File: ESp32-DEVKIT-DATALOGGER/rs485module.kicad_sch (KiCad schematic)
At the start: 17 parts, among them J301 RJ45, U301 MAX485E, U302 MAX3486

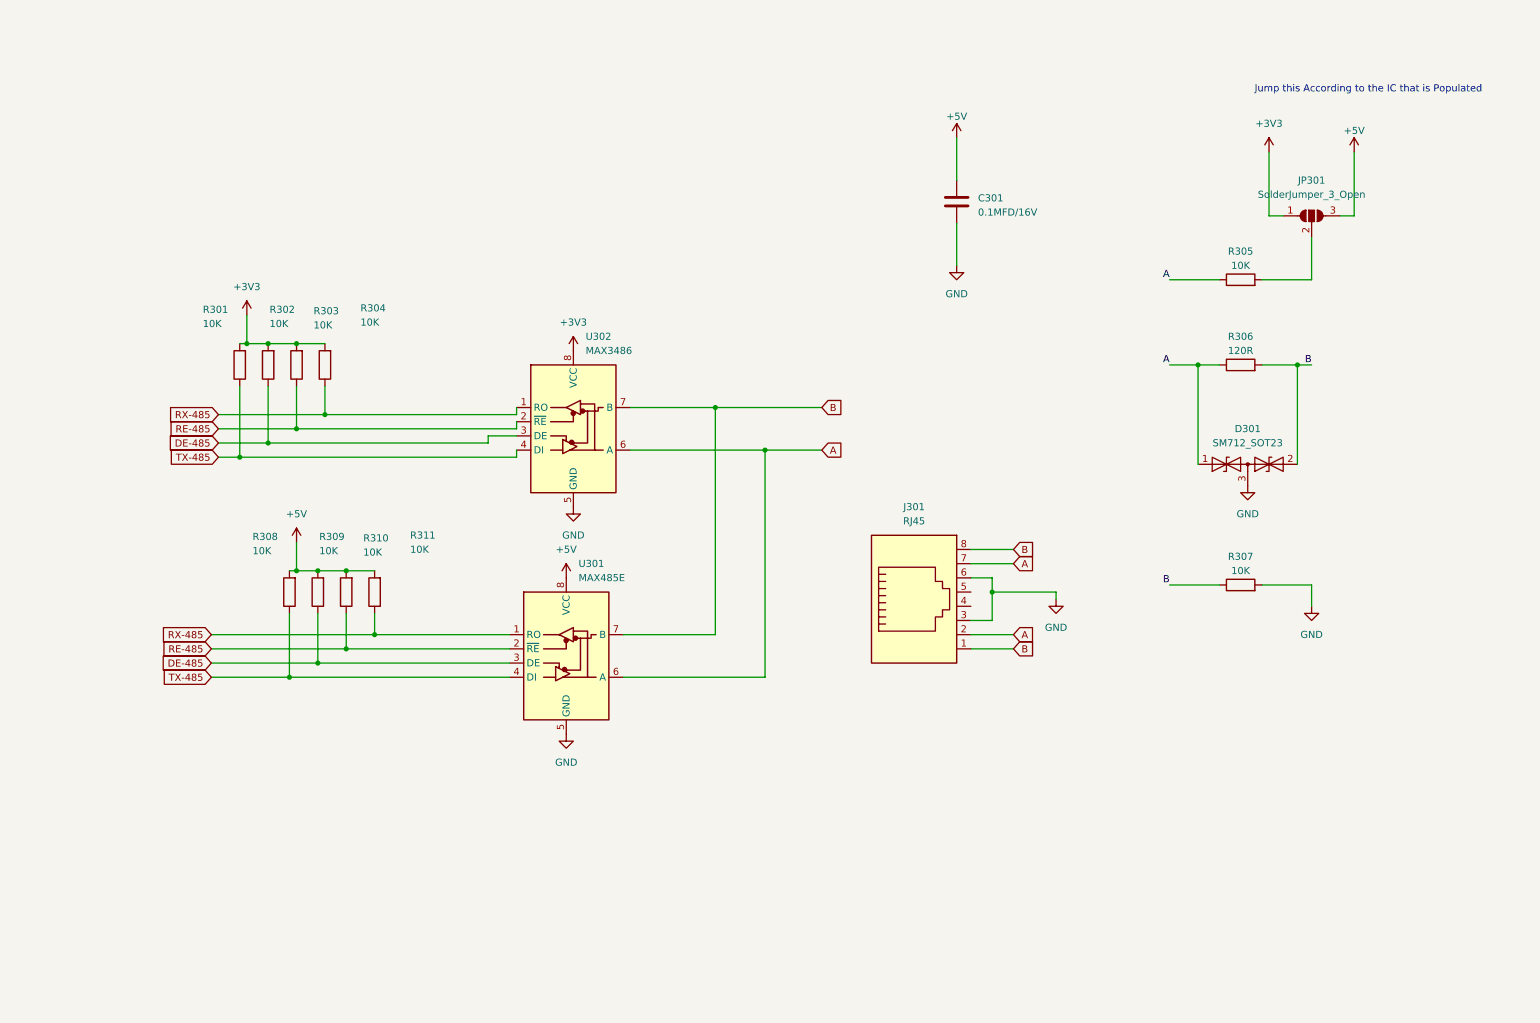
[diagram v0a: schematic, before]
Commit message: Small Changes
Adding I2C components
More RS485
And it is required changing the  Labels for RS485 . for 3 different channels
And Make them ISO Pins
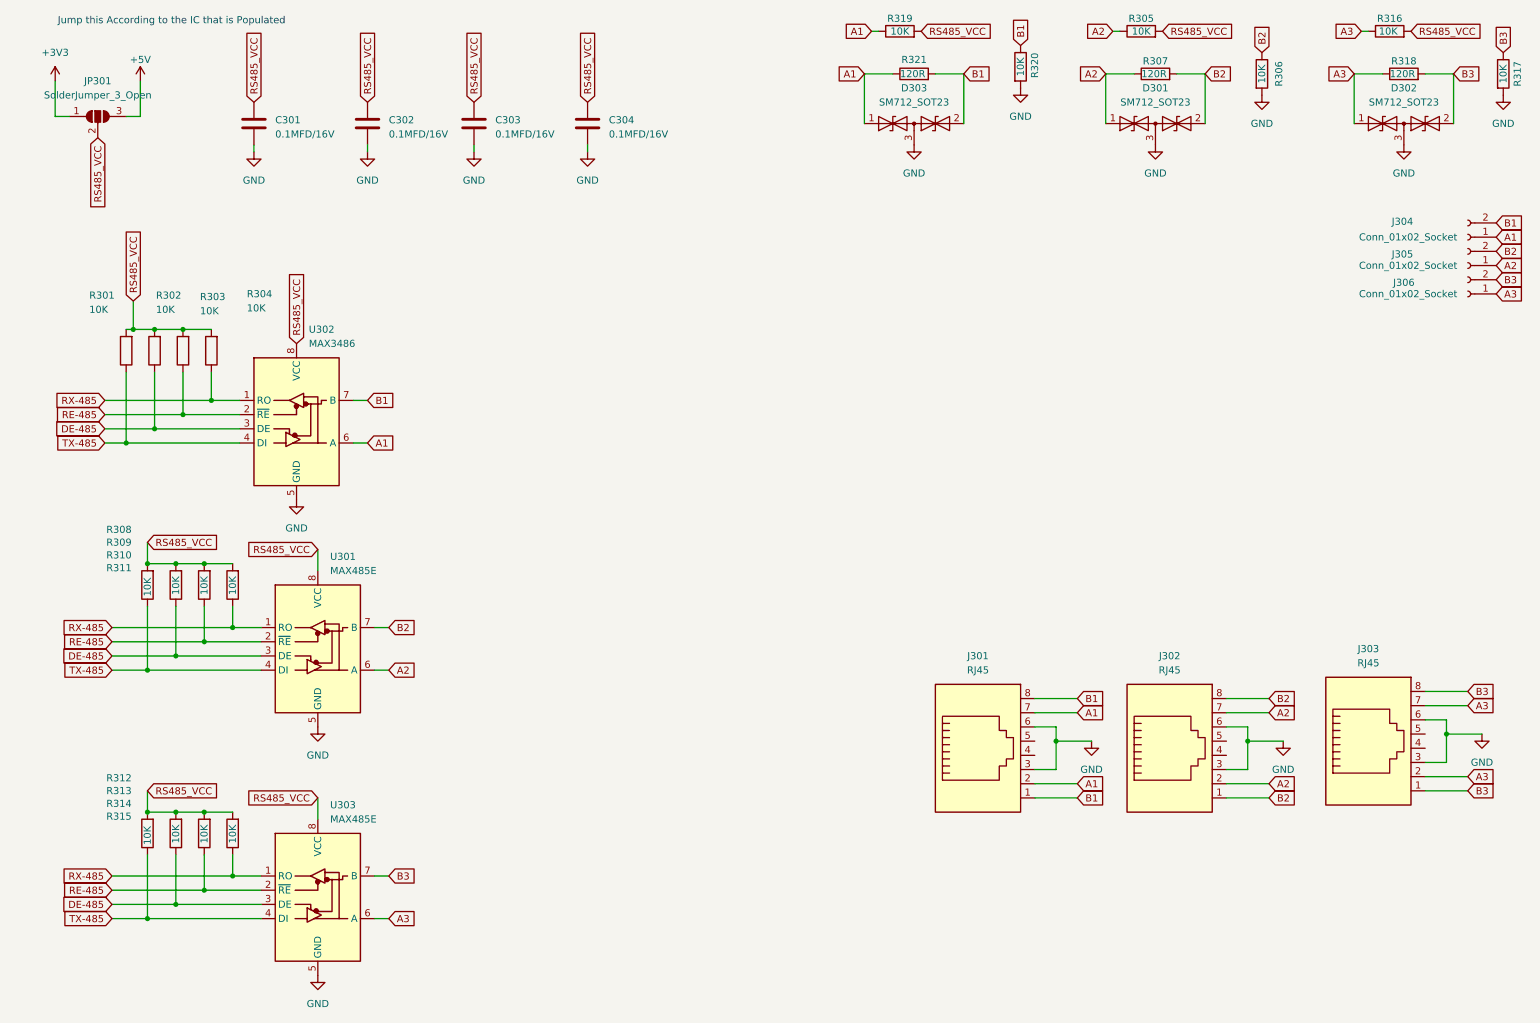
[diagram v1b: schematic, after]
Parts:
- added C302, C303, C304: 0.1MFD/16V, Capacitor_SMD:C_0603_1608Metric_Pad1.08x0.95mm_HandSolder, symbol Device:C
- added D302, D303: SM712_SOT23, Package_TO_SOT_SMD:SOT-23, symbol Diode:SM712_SOT23
- added J302, J303: RJ45, Connector_RJ:RJ45_Amphenol_54602-x08_Horizontal, symbol Connector:RJ45
- added J304, J305, J306: Conn_01x02_Socket, Connector_Molex:Molex_KK-254_AE-6410-02A_1x02_P2.54mm_Vertical, symbol Connector:Conn_01x02_Socket
- added R312, R313, R314, R315, R316, R317, R319, R320: 10K, Resistor_SMD:R_0603_1608Metric_Pad0.98x0.95mm_HandSolder, symbol Device:R
- added R318, R321: 120R, Resistor_SMD:R_0603_1608Metric_Pad0.98x0.95mm_HandSolder, symbol Device:R
- added U303: MAX485E, Package_DIP:DIP-8_W7.62mm_LongPads, symbol Interface_UART:MAX485E
- R306: value 120R -> 10K
- R307: value 10K -> 120R
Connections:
- net +3V3: no longer R301.2, R302.2, R303.2, R304.2, U302.8 (VCC)
- net +5V: no longer C301.1, R308.2, R309.2, R310.2, R311.2, U301.8 (VCC)
- net DE-485: now also R313.1, U303.3 (DE)
- net GND: now also R306.2, C302.2, C303.2, C304.2, D302.3 (common), D303.3 (common), J302.3, J302.6, J303.3, J303.6, R317.2, R320.2, U303.5 (GND); no longer R307.2
- net RE-485: now also R314.1, U303.2 (~{RE})
- net RX-485: now also R315.1, U303.1 (RO)
- net TX-485: now also R312.1, U303.4 (DI)
- net RS485_VCC: now reaches JP301.2 (C), R305.2
- net RS485_VCC: now also C301.1, R301.2, R302.2, R303.2, R304.2, R308.2, R309.2, R310.2, R311.2, U301.8 (VCC), U302.8 (VCC), C302.1, C303.1, C304.1, R312.2, R313.2, R314.2, R315.2, R316.2, R319.2, U303.8 (VCC)
- removed net A: D301.1 (A1), J301.2, J301.7, R305.1, R306.1, U301.6 (A), U302.6 (A)
- removed net B: D301.2 (A2), J301.1, J301.8, R306.2, R307.1, U301.7 (B), U302.7 (B)
- new net A1: D303.1 (A1), J301.2, J301.7, J304.1 (Pin_1), R319.1, R321.1, U302.6 (A)
- new net A2: D301.1 (A1), J302.2, J302.7, J305.1 (Pin_1), R305.1, R307.1, U301.6 (A)
- new net A3: D302.1 (A1), J303.2, J303.7, J306.1 (Pin_1), R316.1, R318.1, U303.6 (A)
- new net B1: D303.2 (A2), J301.1, J301.8, J304.2 (Pin_2), R320.1, R321.2, U302.7 (B)
- new net B2: D301.2 (A2), J302.1, J302.8, J305.2 (Pin_2), R306.1, R307.2, U301.7 (B)
- new net B3: D302.2 (A2), J303.1, J303.8, J306.2 (Pin_2), R317.1, R318.2, U303.7 (B)
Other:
- moved on the sheet: J301, R301, R302, R303, R304, R308, R309, R310, R311, U301, U302
